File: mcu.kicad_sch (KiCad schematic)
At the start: 41 parts, among them SW1 SW_Nidec_CAS-120A1, SW2 CK_KMS2xxG, U1 STM32U5G9ZJTxQ, Y1 Crystal_GND24, Y2 Crystal

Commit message: Assign 0603 footprint to all capacitors
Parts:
- C10, C11, C12, C13, C14, C15, C16, C17, C18, C19, C20, C21, C22, C23, C24, C25, C26, C27, C28, C29, C30, C31, C32, C33, C34, C35, C36, C5, C6, C7, C8, C9: footprint (none) -> Capacitor_SMD:C_0603_1608Metric_Pad1.08x0.95mm_HandSolder
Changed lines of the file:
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@@
 			)
 		)
-		(property "Footprint" ""
+		(property "Footprint" "Capacitor_SMD:C_0603_1608Metric_Pad1.08x0.95mm_HandSolder"
 			(at 163.5252 182.88 0)
 			(effects
@@
 			)
 		)
-		(property "Footprint" ""
+		(property "Footprint" "Capacitor_SMD:C_0603_1608Metric_Pad1.08x0.95mm_HandSolder"
 			(at 93.6752 264.16 0)
 			(effects
@@
 			)
 		)
-		(property "Footprint" ""
+		(property "Footprint" "Capacitor_SMD:C_0603_1608Metric_Pad1.08x0.95mm_HandSolder"
 			(at 112.7252 182.88 0)
 			(effects
@@
 			)
 		)
-		(property "Footprint" ""
+		(property "Footprint" "Capacitor_SMD:C_0603_1608Metric_Pad1.08x0.95mm_HandSolder"
 			(at 82.2452 163.83 0)
 			(effects
@@
 			)
 		)
-		(property "Footprint" ""
+		(property "Footprint" "Capacitor_SMD:C_0603_1608Metric_Pad1.08x0.95mm_HandSolder"
 			(at 82.2452 93.98 0)
 			(effects
@@
 			)
 		)
-		(property "Footprint" ""
+		(property "Footprint" "Capacitor_SMD:C_0603_1608Metric_Pad1.08x0.95mm_HandSolder"
 			(at 122.8852 182.88 0)
 			(effects
@@
 			)
 		)
-		(property "Footprint" ""
+		(property "Footprint" "Capacitor_SMD:C_0603_1608Metric_Pad1.08x0.95mm_HandSolder"
 			(at 82.2452 182.88 0)
 			(effects
@@
 			)
 		)
-		(property "Footprint" ""
+		(property "Footprint" "Capacitor_SMD:C_0603_1608Metric_Pad1.08x0.95mm_HandSolder"
 			(at 143.2052 182.88 0)
 			(effects
@@
 			)
 		)
-		(property "Footprint" ""
+		(property "Footprint" "Capacitor_SMD:C_0603_1608Metric_Pad1.08x0.95mm_HandSolder"
 			(at 92.4052 163.83 0)
 			(effects
@@
 			)
 		)
-		(property "Footprint" ""
+		(property "Footprint" "Capacitor_SMD:C_0603_1608Metric_Pad1.08x0.95mm_HandSolder"
 			(at 102.5652 182.88 0)
 			(effects
@@
 			)
 		)
-		(property "Footprint" ""
+		(property "Footprint" "Capacitor_SMD:C_0603_1608Metric_Pad1.08x0.95mm_HandSolder"
 			(at 133.0452 182.88 0)
 			(effects
@@
 			)
 		)
-		(property "Footprint" ""
+		(property "Footprint" "Capacitor_SMD:C_0603_1608Metric_Pad1.08x0.95mm_HandSolder"
 			(at 112.7252 207.01 0)
 			(effects
@@
 			)
 		)
-		(property "Footprint" ""
+		(property "Footprint" "Capacitor_SMD:C_0603_1608Metric_Pad1.08x0.95mm_HandSolder"
 			(at 183.8452 182.88 0)
 			(effects
@@
 			)
 		)
-		(property "Footprint" ""
+		(property "Footprint" "Capacitor_SMD:C_0603_1608Metric_Pad1.08x0.95mm_HandSolder"
 			(at 72.0852 241.3 0)
 			(effects
@@
 			)
 		)
-		(property "Footprint" ""
+		(property "Footprint" "Capacitor_SMD:C_0603_1608Metric_Pad1.08x0.95mm_HandSolder"
 			(at 92.4052 129.54 0)
 			(effects
@@
 			)
 		)
-		(property "Footprint" ""
+		(property "Footprint" "Capacitor_SMD:C_0603_1608Metric_Pad1.08x0.95mm_HandSolder"
 			(at 92.4052 111.76 0)
 			(effects
@@
 			)
 		)
-		(property "Footprint" ""
+		(property "Footprint" "Capacitor_SMD:C_0603_1608Metric_Pad1.08x0.95mm_HandSolder"
 			(at 82.2452 54.61 0)
 			(effects
@@
 			)
 		)
-		(property "Footprint" ""
+		(property "Footprint" "Capacitor_SMD:C_0603_1608Metric_Pad1.08x0.95mm_HandSolder"
 			(at 82.2452 111.76 0)
 			(effects
@@
 			)
 		)
-		(property "Footprint" ""
+		(property "Footprint" "Capacitor_SMD:C_0603_1608Metric_Pad1.08x0.95mm_HandSolder"
 			(at 223.2152 69.85 0)
 			(effects
@@
 			)
 		)
-		(property "Footprint" ""
+		(property "Footprint" "Capacitor_SMD:C_0603_1608Metric_Pad1.08x0.95mm_HandSolder"
 			(at 82.2452 74.93 0)
 			(effects
@@
 			)
 		)
-		(property "Footprint" ""
+		(property "Footprint" "Capacitor_SMD:C_0603_1608Metric_Pad1.08x0.95mm_HandSolder"
 			(at 92.4052 147.32 0)
 			(effects
@@
 			)
 		)
-		(property "Footprint" ""
+		(property "Footprint" "Capacitor_SMD:C_0603_1608Metric_Pad1.08x0.95mm_HandSolder"
 			(at 82.2452 129.54 0)
 			(effects
@@
 			)
 		)
-		(property "Footprint" ""
+		(property "Footprint" "Capacitor_SMD:C_0603_1608Metric_Pad1.08x0.95mm_HandSolder"
 			(at 93.6752 241.3 0)
 			(effects
@@
 			)
 		)
-		(property "Footprint" ""
+		(property "Footprint" "Capacitor_SMD:C_0603_1608Metric_Pad1.08x0.95mm_HandSolder"
 			(at 92.4052 182.88 0)
 			(effects
@@
 			)
 		)
-		(property "Footprint" ""
+		(property "Footprint" "Capacitor_SMD:C_0603_1608Metric_Pad1.08x0.95mm_HandSolder"
 			(at 173.6852 182.88 0)
 			(effects
@@
 			)
 		)
-		(property "Footprint" ""
+		(property "Footprint" "Capacitor_SMD:C_0603_1608Metric_Pad1.08x0.95mm_HandSolder"
 			(at 82.2452 147.32 0)
 			(effects
@@
 			)
 		)
-		(property "Footprint" ""
+		(property "Footprint" "Capacitor_SMD:C_0603_1608Metric_Pad1.08x0.95mm_HandSolder"
 			(at 102.5652 163.83 0)
 			(effects
@@
 			)
 		)
-		(property "Footprint" ""
+		(property "Footprint" "Capacitor_SMD:C_0603_1608Metric_Pad1.08x0.95mm_HandSolder"
 			(at 91.1352 207.01 0)
 			(effects
@@
 			)
 		)
-		(property "Footprint" ""
+		(property "Footprint" "Capacitor_SMD:C_0603_1608Metric_Pad1.08x0.95mm_HandSolder"
 			(at 153.3652 182.88 0)
 			(effects
@@
 			)
 		)
-		(property "Footprint" ""
+		(property "Footprint" "Capacitor_SMD:C_0603_1608Metric_Pad1.08x0.95mm_HandSolder"
 			(at 79.7052 207.01 0)
 			(effects
@@
 			)
 		)
-		(property "Footprint" ""
+		(property "Footprint" "Capacitor_SMD:C_0603_1608Metric_Pad1.08x0.95mm_HandSolder"
 			(at 101.2952 207.01 0)
 			(effects
@@
 			)
 		)
-		(property "Footprint" ""
+		(property "Footprint" "Capacitor_SMD:C_0603_1608Metric_Pad1.08x0.95mm_HandSolder"
 			(at 72.0852 264.16 0)
 			(effects

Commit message: Assign 0603 footprints to all resistors
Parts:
- R5, R6: footprint (none) -> Resistor_SMD:R_0603_1608Metric_Pad0.98x0.95mm_HandSolder
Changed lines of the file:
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@@
 			)
 		)
-		(property "Footprint" ""
+		(property "Footprint" "Resistor_SMD:R_0603_1608Metric_Pad0.98x0.95mm_HandSolder"
 			(at 339.852 161.29 90)
 			(effects
@@
 			)
 		)
-		(property "Footprint" ""
+		(property "Footprint" "Resistor_SMD:R_0603_1608Metric_Pad0.98x0.95mm_HandSolder"
 			(at 222.25 112.268 90)
 			(effects

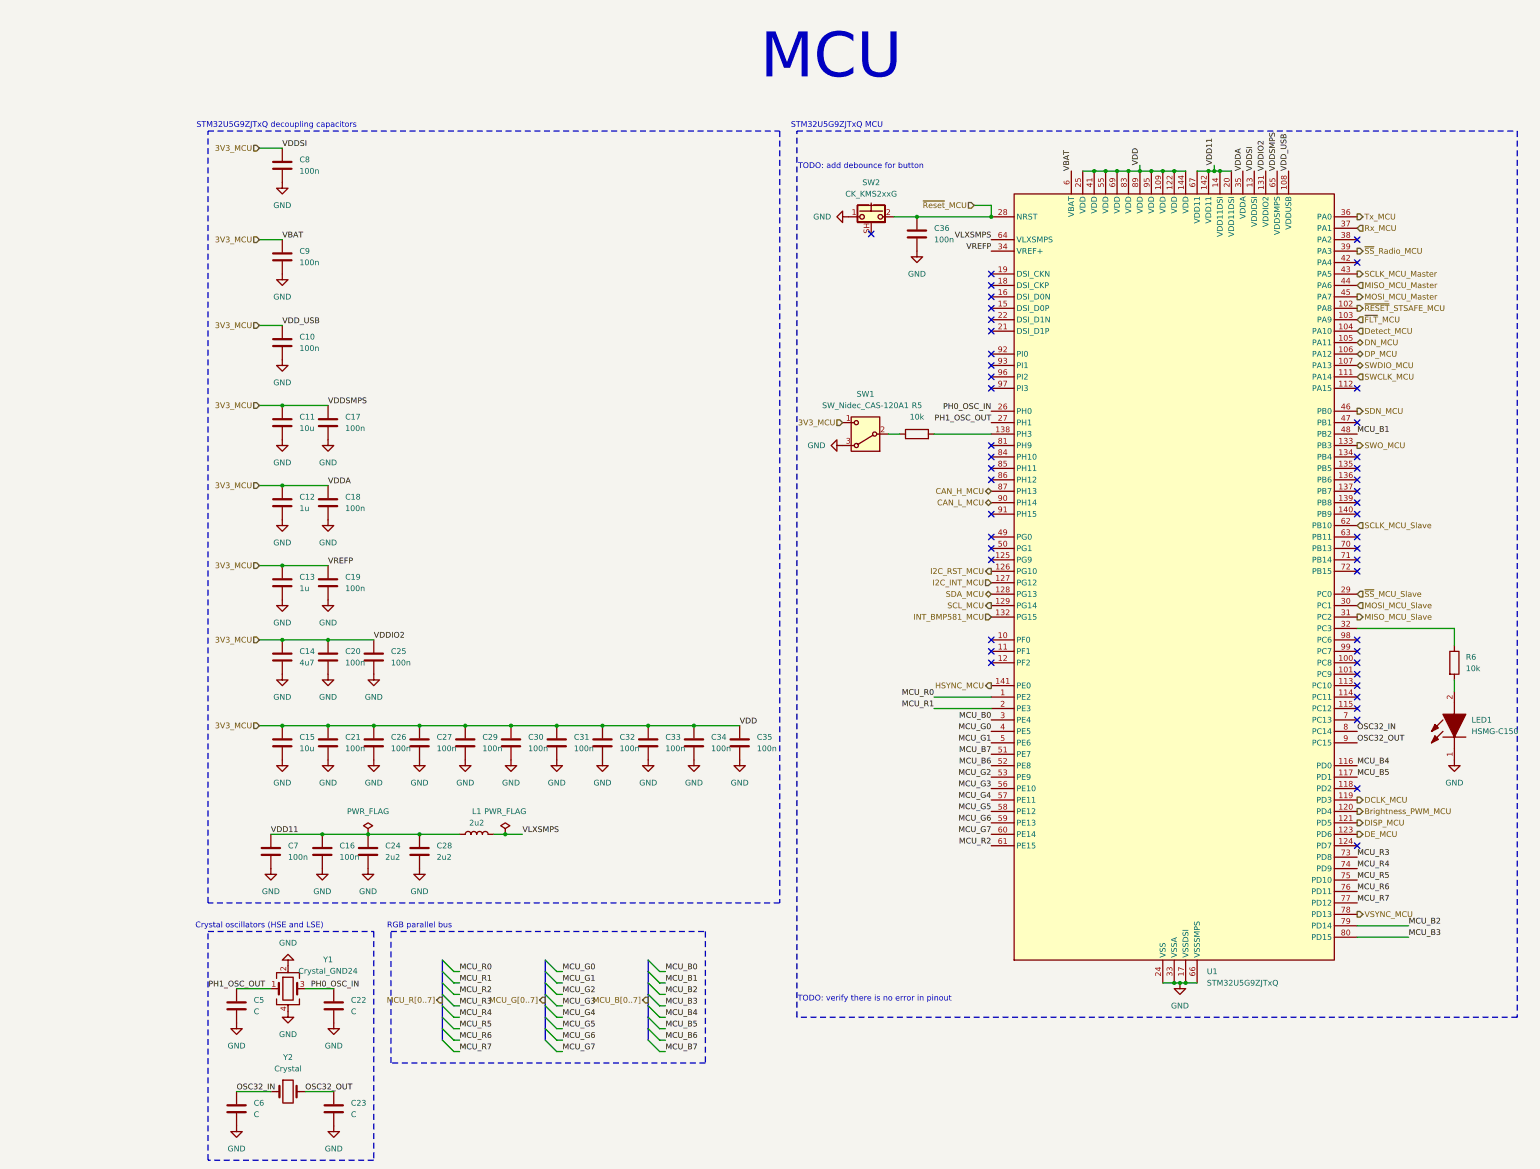
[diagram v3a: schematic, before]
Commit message: Setup crystal oscillators for MCU and S2LP
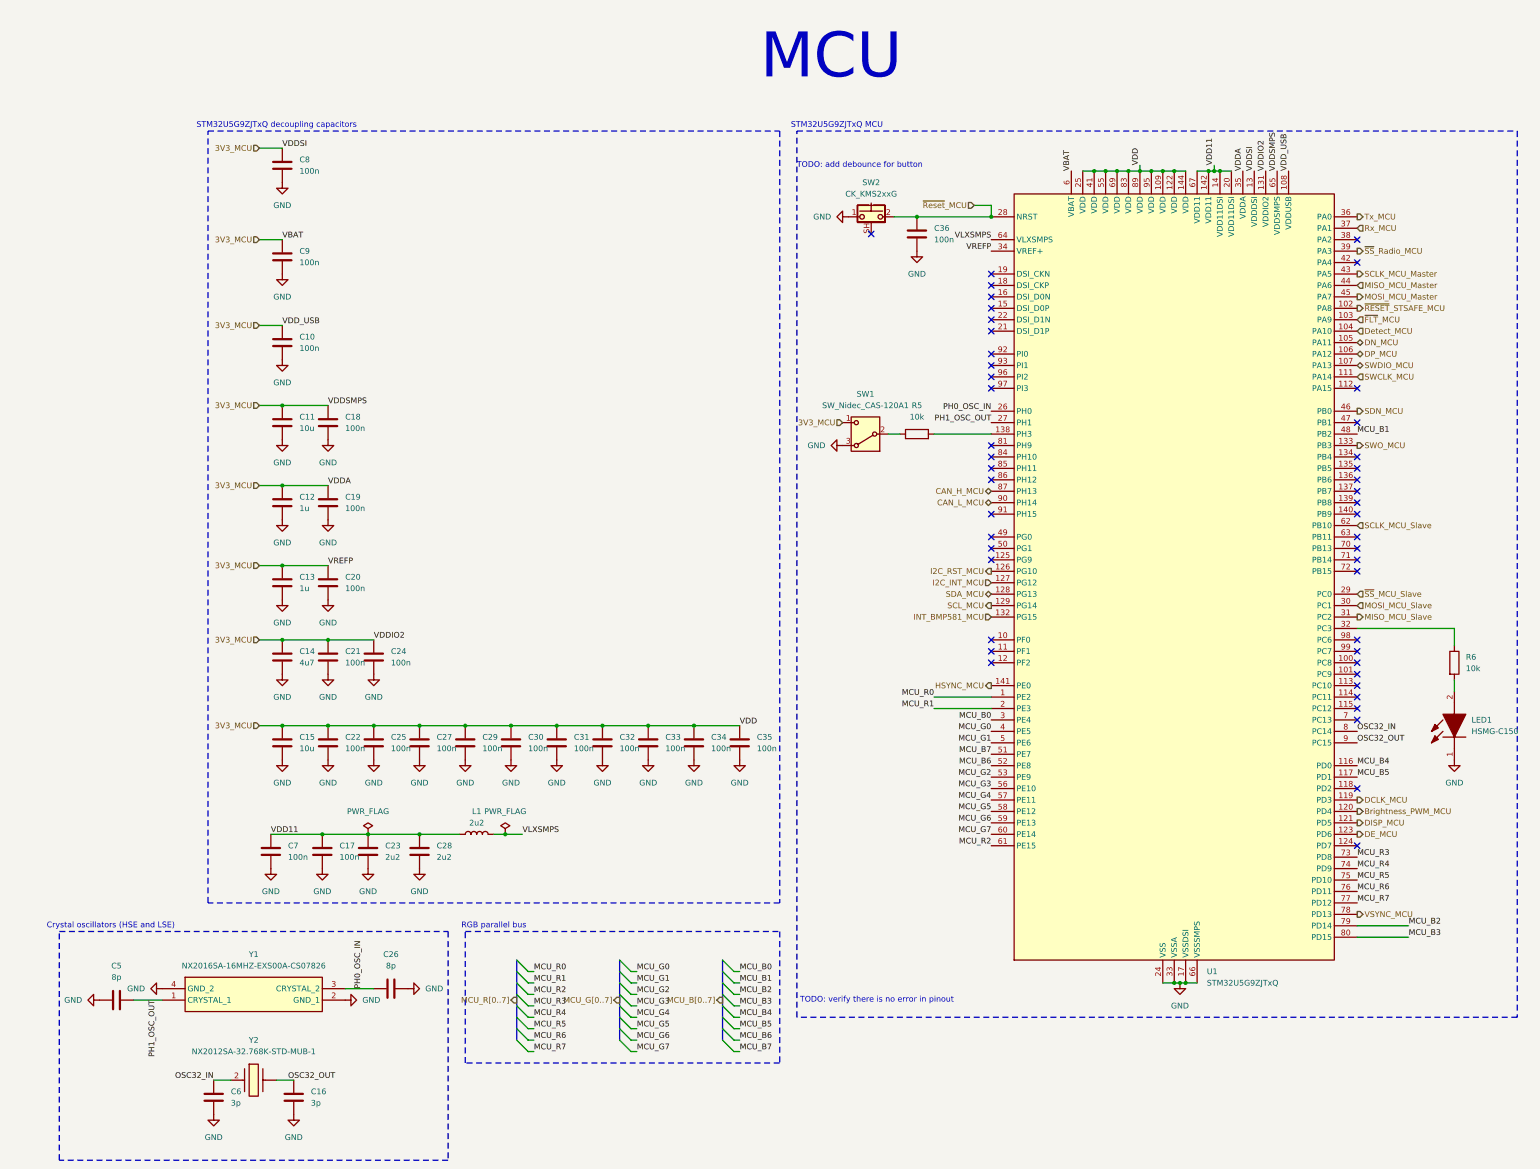
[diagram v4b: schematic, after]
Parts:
- removed Y1: Crystal_GND24, symbol Device:Crystal_GND24
- removed Y2: Crystal, symbol Device:Crystal
- added Y1: NX2016SA-16MHZ-EXS00A-CS07826, weather-station-poc-fp:NX2016SA16MHZEXS00ACS07826, symbol weather-station-poc-sym:NX2016SA-16MHZ-EXS00A-CS07826
- added Y2: NX2012SA-32.768K-STD-MUB-1, weather-station-poc-fp:NX2012SA32768KSTDMUB1, symbol weather-station-poc-sym:NX2012SA-32.768K-STD-MUB-1
- C16: renamed from C23; value C -> 3p
- C26: renamed from C22; value C -> 8p
- C5: value C -> 8p
- C6: value C -> 3p
- renumbered C16 to C17, C17 to C18, C18 to C19, C19 to C20, C20 to C21, C21 to C22, C24 to C23, C25 to C24, C26 to C25
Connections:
- net GND: now also C5.1, Y1.2 (GND_1), Y1.4 (GND_2); no longer C5.2
- net OSC32_IN: now also Y2.2 (CRYSTAL_2)
- net OSC32_OUT: now also Y2.
- net PH0_OSC_IN: now also Y1.3 (CRYSTAL_2)
- net PH1_OSC_OUT: now also C5.2, Y1.1 (CRYSTAL_1); no longer C5.1
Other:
- moved on the sheet: C16, C26, C5, C6
